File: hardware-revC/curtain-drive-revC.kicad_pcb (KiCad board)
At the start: 2 copper layers, 90 x 72 mm, 49 parts, among them J1 12V IN, J3 MOTOR, J4 ENCODER I2C, J5 UART, SW1 USER, SW2 BOOT, SW3 RESET, U1 ESP32-WROOM-32, U2 L298, U3 LM2575T-ADJ, U4 LM7805

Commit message: Rev C: proven LM317 supply for the WROOM-32, 470 uF at the module
Rework rev C to the ESP32 recipe that ran on real hardware
(esp32-solder-test). The LM2575 buck was untested with the shop's 120 uH
inductor; the 3.3 V rail now comes from an LM317T (243R/392R, 3.27 V) fed
from 12 V through a 1N5817, with a 1N4003 reverse-protection diode, 10 uF +
100 nF at its input and 10 uF at its output. It needs the shop's TO-220
heatsink at 12 V, and its tab faces a cleared area at the bottom edge.

The 470 uF bulk cap moves onto the module's 3V3 line, on a 0.8 mm track:
a 10 uF rail collapsed under the Wi-Fi TX peaks on the test board. IO0
gets its 10k pull-up (R15), and the firmware caps TX power at 8.5 dBm.

Re-routed with FreeRouting, 0 unconnected and DRC clean apart from silk
and courtyard margins. Laser and per-layer DXFs, drill file, schematic PDF
and BOM regenerated.

Co-Authored-By: Claude Opus 5.5 (1M context) <noreply@anthropic.com>
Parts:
- removed L1: 120uH 1A, Inductor_THT:L_Radial_D10.0mm_P5.00mm_Fastron_07M
- added D10: 1N4003, Diode_THT:D_DO-41_SOD81_P10.16mm_Horizontal, B.Cu at (176.2, 152.0)
- added R15: 10k, Resistor_THT:R_Axial_DIN0207_L6.3mm_D2.5mm_P7.62mm_Horizontal, B.Cu at (165.1, 129.5)
- C4: value 47uF 50V -> 10uF 50V; footprint Capacitor_THT:CP_Radial_D6.3mm_P2.50mm -> Capacitor_THT:CP_Radial_D5.0mm_P2.00mm
- R17: value 1.69k -> 243
- R18: value 1.00k -> 392
- U3: value LM2575T-ADJ -> LM317T; footprint CurtainDrive:TO-220-5_Vertical_LongPads -> Package_TO_SOT_THT:TO-220-3_Vertical
- moved C7 75.0 mm to (119.3, 106.5), turned to 180 degrees
- moved C10 74.3 mm to (172.0, 147.0), turned to 0 degrees
- moved C4 22.1 mm to (178.0, 160.0), turned to 0 degrees
- moved R18 22.0 mm to (159.5, 155.3), turned to 90 degrees
- moved C8 15.4 mm to (178.0, 164.0), turned to 0 degrees
- moved D2 14.9 mm to (162.2, 169.0), turned to 180 degrees
- moved U3 7.81 mm to (167.0, 158.0)
- moved R17 7.50 mm to (169.1, 155.3), turned to 180 degrees
- moved C11 4.50 mm to (112.0, 102.5)
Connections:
- C4 pad 1: +12V -> Net-(D10-K)
- C8 pad 1: +3V3 -> Net-(D10-K)
- D2 pad 1: Net-(D2-K) -> Net-(D10-K)
- D2 pad 2: GND -> +12V
- R17 pad 2: Net-(U3-FB) -> Net-(U3-ADJ)
- R18 pad 1: Net-(U3-FB) -> Net-(U3-ADJ)
- U3 pad 1: +12V -> Net-(U3-ADJ)
- U3 pad 2: Net-(D2-K) -> +3V3
- U3 pad 3: GND -> Net-(D10-K)
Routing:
- net Net-(D10-K): track 0.00 -> 35.8 mm
- net +12V: track 160.8 -> 140.7 mm
- net Net-(D2-K): track 19.0 -> 0.00 mm
- net +3V3: track 176.8 -> 193.2 mm
- net Net-(U3-FB): track 12.8 -> 0.00 mm
- net Net-(U3-ADJ): track 0.00 -> 8.62 mm
- net SDA: track 42.3 -> 41.2 mm

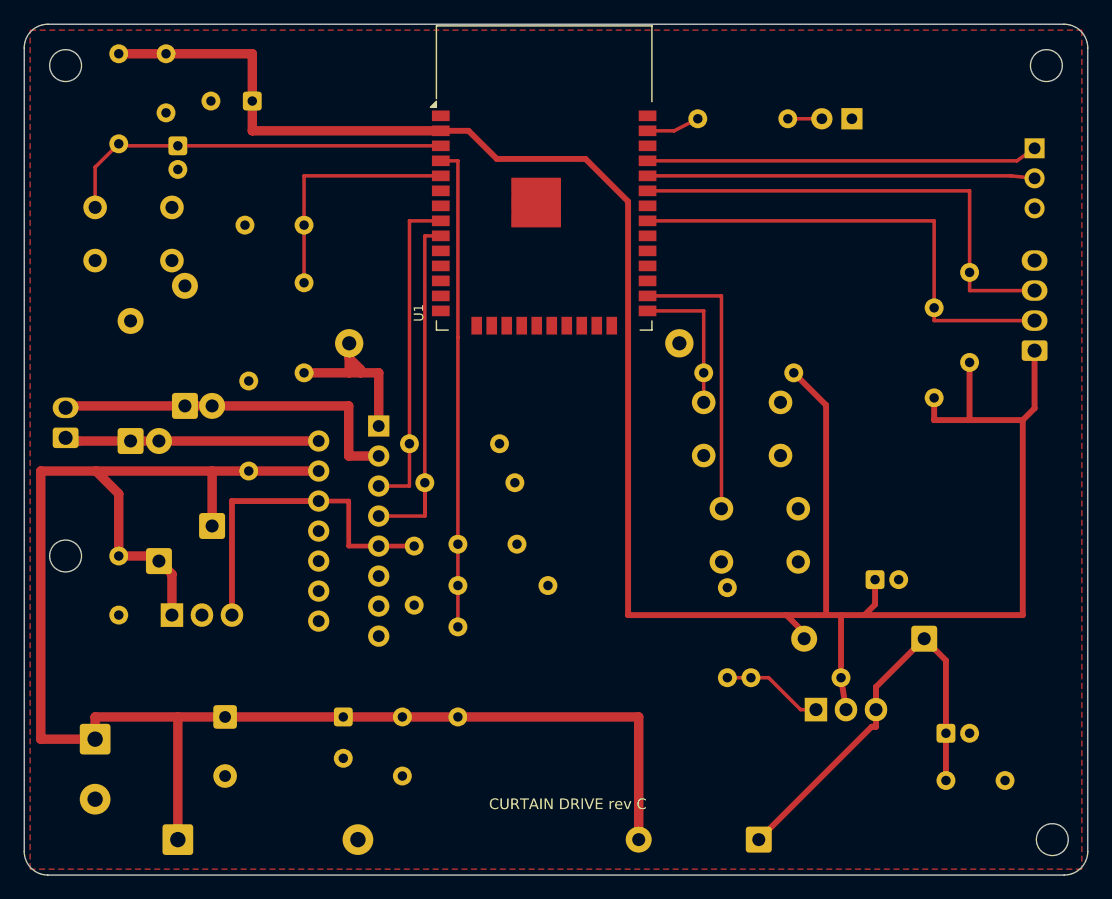
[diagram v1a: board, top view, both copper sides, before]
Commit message: Rev C: pin holes and keep-out for U3's pin-mount heatsink
The shop's TO-220 heatsink (16 x 16 x 25.4 mm) stands on two 2.3 mm pins,
10.2 mm apart, with their centres 2.5 mm behind the face the LM317's tab
bolts to. U3 gets its own footprint with those two 2.6 mm unplated holes
(5.65 mm behind the leg row, centred on OUT) and a courtyard covering the
heatsink, so the laser cut file carries the holes and no part lands under it.

U3 moves up to y = 52 so the heatsink ends inside the board edge; R17, R18,
D10, C10, C4 and C8 re-placed around it. Re-routed: 0 unconnected, DRC
clean apart from silk and courtyard margins. DXFs, drill file, PDF and
build notes regenerated.

Co-Authored-By: Claude Opus 5.5 (1M context) <noreply@anthropic.com>
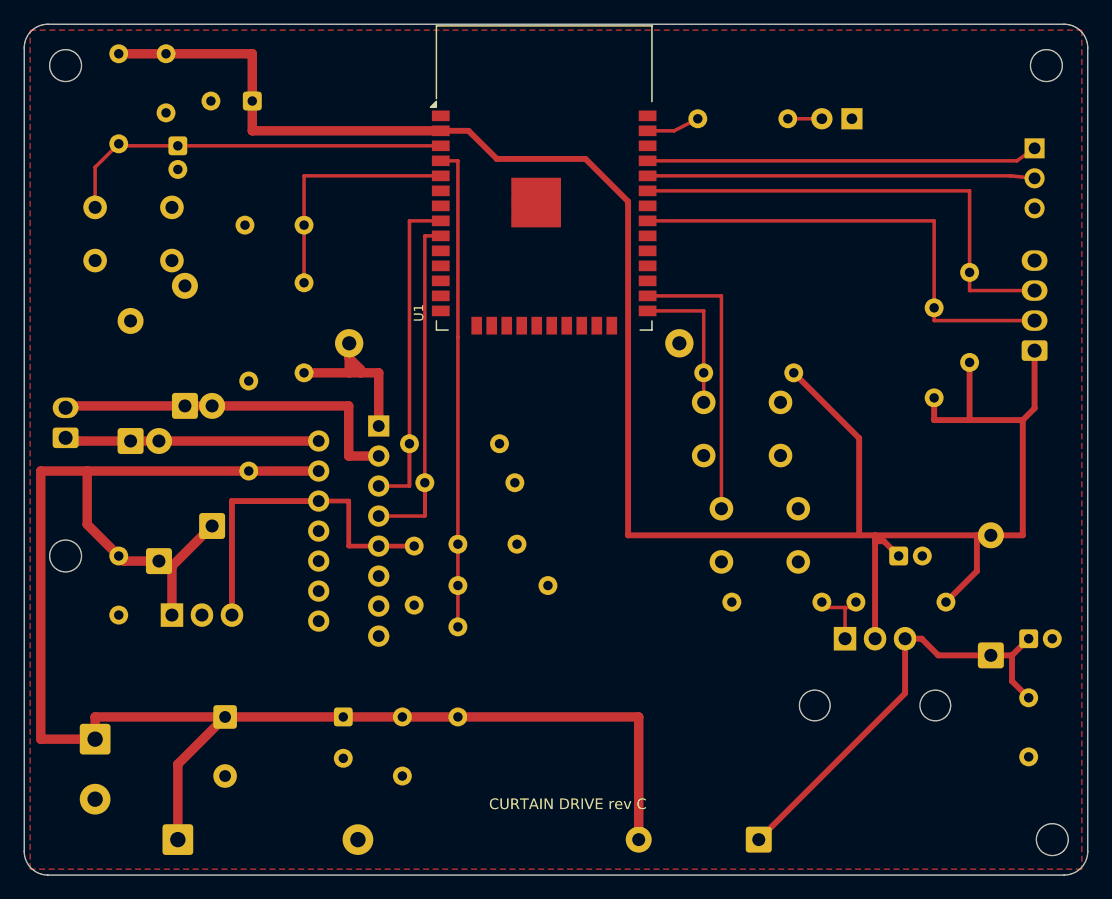
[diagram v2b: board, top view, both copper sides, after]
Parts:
- U3: footprint Package_TO_SOT_THT:TO-220-3_Vertical -> CurtainDrive:TO-220-3_Vertical_Heatsink16x16
- moved R17 10.9 mm to (178.0, 148.9)
- moved C4 10.6 mm to (185.0, 152.0)
- moved R18 10.2 mm to (167.5, 148.9), turned to 180 degrees
- moved C8 9.90 mm to (185.0, 157.0), turned to -90 degrees
- moved U3 6.48 mm to (169.5, 152.0)
- moved D10 5.81 mm to (181.8, 153.4), turned to 90 degrees
- moved C10 2.83 mm to (174.0, 145.0)
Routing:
- net +3V3: track 193.2 -> 178.1 mm
- net M_IN1: track 27.7 -> 31.3 mm
- net Net-(U3-ADJ): track 8.62 -> 5.90 mm
- net +12V: track 140.7 -> 143.2 mm
- net Net-(D10-K): track 35.8 -> 37.9 mm
